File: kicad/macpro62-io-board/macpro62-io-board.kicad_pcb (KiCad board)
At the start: 6 copper layers, 101 x 173.6 mm, 146 parts, among them J1 IOB-HS1 MCIO 124 RA <- CB J3 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, J2 DISPLAY-LINK MCIO 74 RA <- Fa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, J25 ETH1 i226-V #1: ZJLQ-RJ45-SMD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, J26 ETH2 i226-V #2: ZJLQ-RJ45-SMD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, J28 Stock audio module connector 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, J29 Speaker 2P (stock lead; pitch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, J3 Stock PSU DC-out 12P (UNCONFI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, J30 Optional stock/remote power b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, J31 I/O-wall (821-2222) flex ZIF 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, J4 Stock PSU signal 6P (UNCONFIR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, J5 PSU pass-through -> BP J2 (12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, J6 IOB-LINK GH15 <- BP J6, J7 CONN_C fan + AirPort 2x20 @0.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, SW1 DNP with the stock 821-2222-A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, SW2 DIAG button, T1 ETH1 2.5G magnetics JASN V24P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, T2 ETH2 2.5G magnetics JASN V24P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, U1 TPS65994AD PD #1 (C1, C2), U11 TUSB1046A C1 alt-mode mux/red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, U12 TUSB1046A C2 alt-mode mux/red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, U13 TUSB1046A C3 alt-mode mux/red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, U14 TUSB1046A C4 alt-mode mux/red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, U15 TUSB1046A C5 alt-mode mux/red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, U16 TUSB1046A C6 alt-mode mux/red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, U2 TPS65994AD PD #2 (C3, C4), U21 TUSB1002A A1 10G redriver, U22 TUSB1002A A2 10G redriver, U23 TUSB1002A A3 10G redriver, U24 TUSB1002A A4 10G redriver, U25 USB-A A1 VBUS switch 1.5 A (S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, U26 USB-A A2 VBUS switch 1.5 A (S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, U27 USB-A A3 VBUS switch 1.5 A (S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, U28 USB-A A4 VBUS switch 1.5 A (S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, U3 TPS65994AD PD #3 (C5, C6), U30 Hall A (DRV5032 class) - posi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, U31 Hall B (DRV5032 class) - posi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, U32 CH334R hub H1b (C4-C6 + codec), U33 CH334R hub H2 (A1-A4) <- IOB-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, U34 CH334R hub H1a (C1-C3 + H1b) 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, U35 CH334R hub H3 on H2 port 4: A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, U4 PD #1 config SPI flash (W25Q8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, U40 TPS259824ON eFuse 12 V in (15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, U41 TPS56C215 5V_C buck (USB-C VB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, U42 TPS56C215 5V_A buck (USB-A VB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, U43 TLV62585 3V3 (3 A) from 5V_SYS, U50 i226-V 2.5GbE (PCIe x1 from H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, U51 i226-V NVM SPI flash (size pe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, U52 i226-V #2 2.5GbE (PCIe x1 fro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, U53 i226-V #2 NVM SPI flash, U6 PD #2 config SPI flash, U60 TDP158 HDMI 2.0 retimer (GPU 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, U61 1V1 LDO (TDP158 core), U7 PD #3 config SPI flash, U70 C-Media CM108B USB audio code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, U71 PAM8302A mono class-D 2.5 W (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, U80 TLC59116 16-ch I2C LED driver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, U81 LIS2DH12 accelerometer (rotat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, U82 BL24C64A IOB ID EEPROM @0x51, U83 TCA9517 I2C buffer (I2C_SYS <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, U84 74LVC1G07 PD_INT -> IOB_INT_N, U90 EMC2101 fan controller @0x4C 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, U91 ASM1182e PCIe Gen2 switch: up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, Y1 12 MHz hub crystal, Y2 12 MHz hub crystal, Y3 12 MHz hub crystal, Y4 25 MHz (i226-V), Y5 12 MHz (CM108B), Y6 25 MHz (i226-V #2), Y7 12 MHz hub crystal (H3)

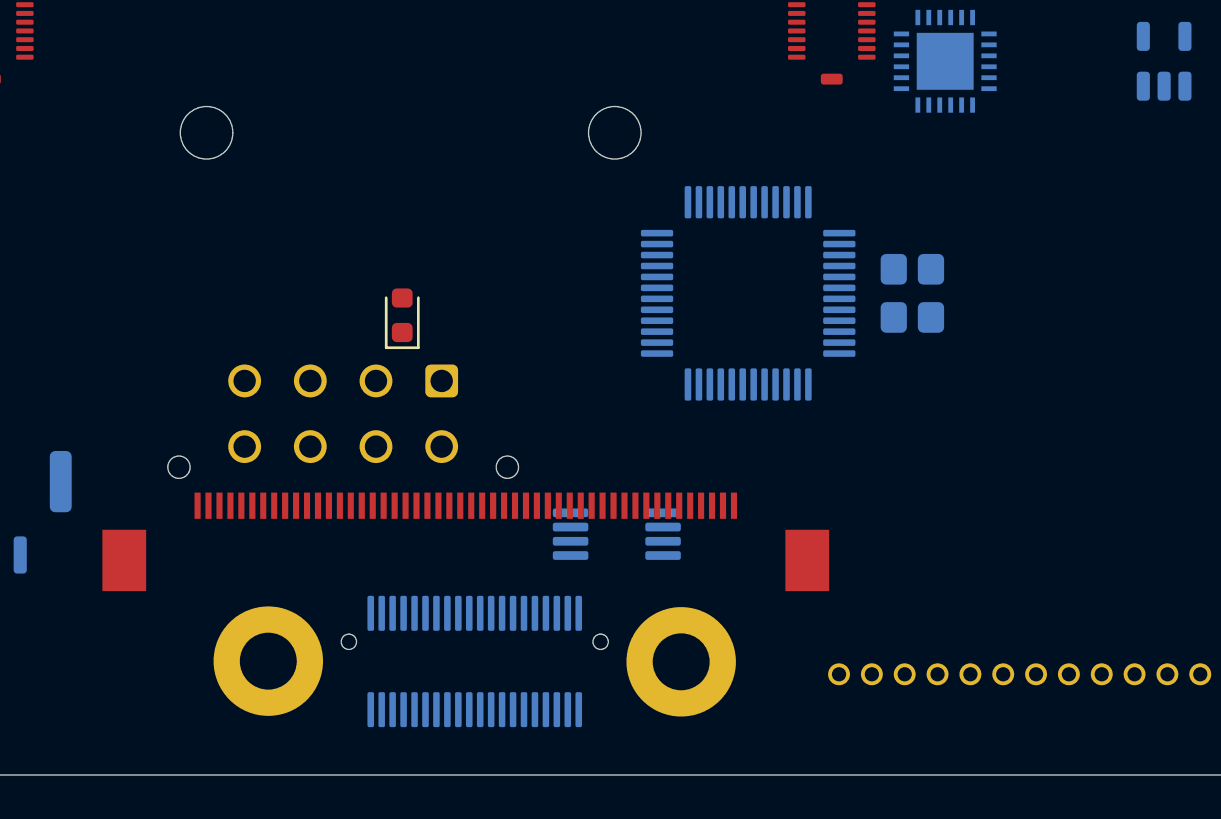
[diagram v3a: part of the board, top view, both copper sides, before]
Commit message: I/O: cover scan check (R inner ~102-110), fan antenna U.FL J8, T8 bracket keep-out, BCM94360 12+6 pinout on CONN_C
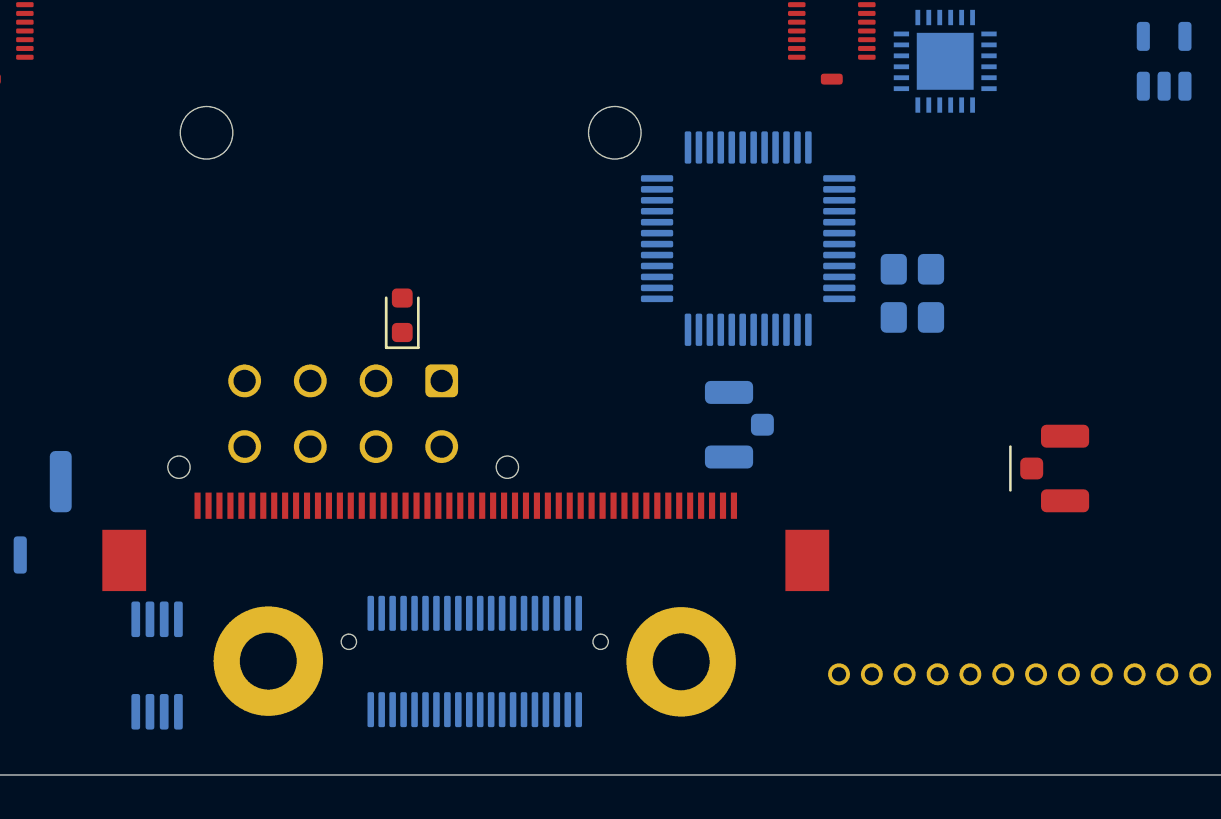
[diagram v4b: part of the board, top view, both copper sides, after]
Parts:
- added J8: Fan-assembly antenna coax: U.FL-R-SMT-1(10) C88373 (stock t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, MP62_IO:MP62_UFL_Hirose_U.FL-R-SMT-1, B.Cu at (102.6, 184.0)
- added J9: Optional antenna pass-through U.FL C88373 (50 ohm CPW from 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, MP62_IO:MP62_UFL_Hirose_U.FL-R-SMT-1, F.Cu at (117.0, 186.0)
- moved U90 21.8 mm to (76.0, 195.0), turned to 90 degrees
- moved U70 2.50 mm to (103.0, 175.5)
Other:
- board text added: "B: T8 fan-cable bracket keep-out (only J7, H14, H15)"

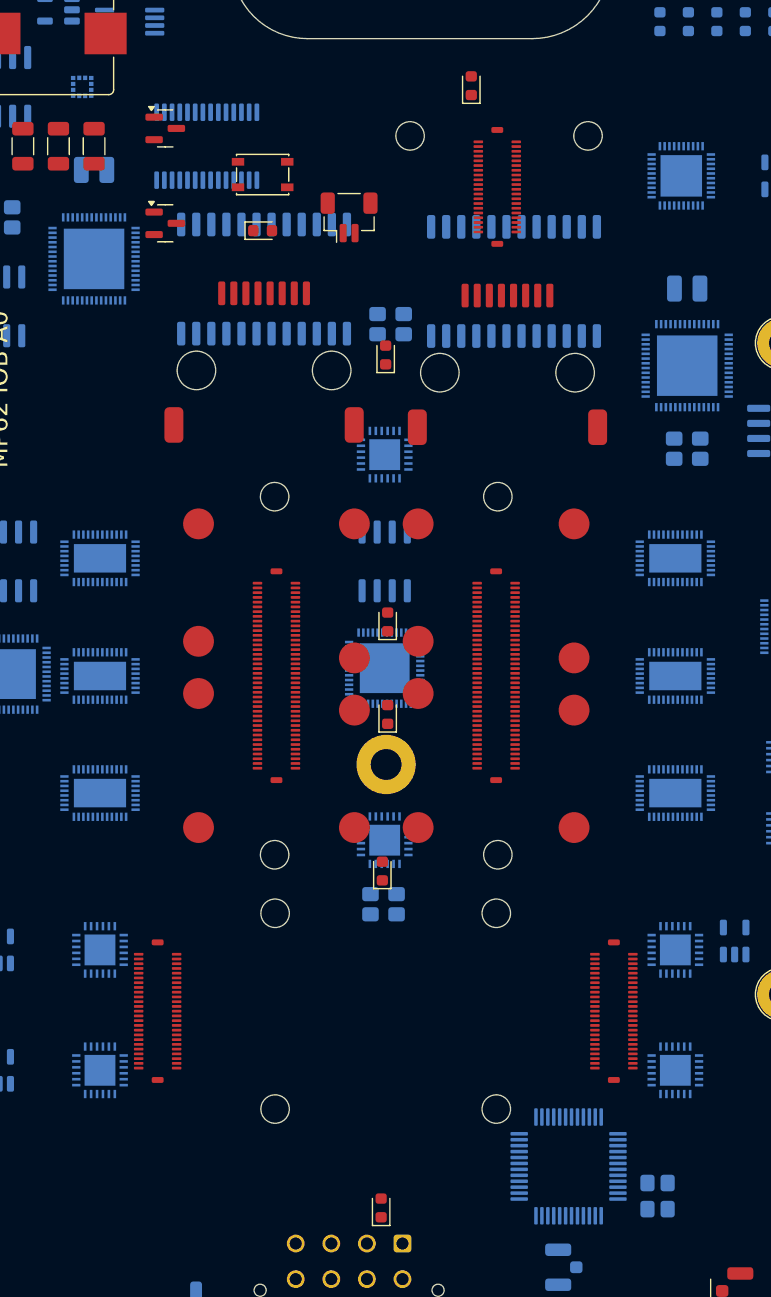
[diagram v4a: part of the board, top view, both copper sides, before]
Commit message: I/O: ports tilted 12.5 deg per stock, riser edge trims, USB-A B2B moved on top, outer-face plug seats, D21-D26 removed
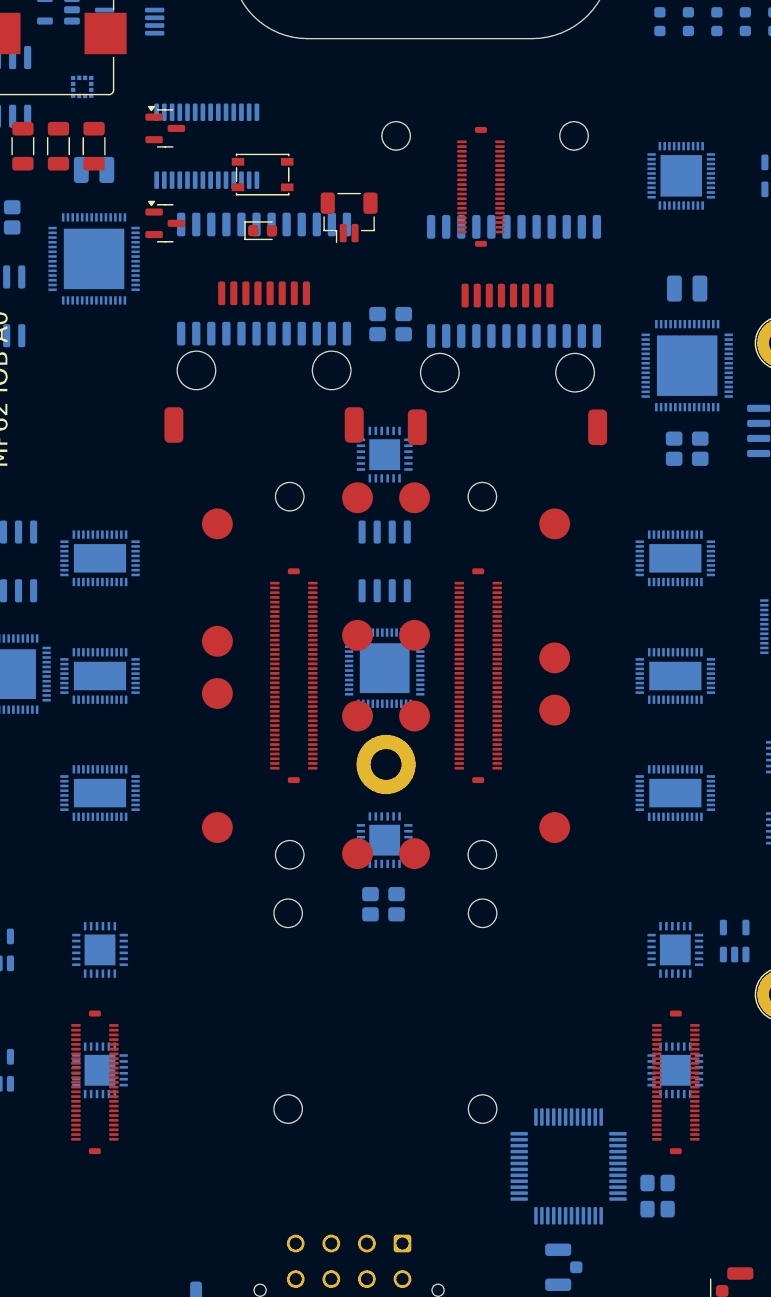
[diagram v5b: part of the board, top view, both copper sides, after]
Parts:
- removed D21: Light-pipe LED: HDMI label - DNP with the stock flex (its o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, MP62_IO:LED_0603_1608Metric
- removed D22: Light-pipe LED: ETH icon - DNP with the stock flex (its own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, MP62_IO:LED_0603_1608Metric
- removed D23: Light-pipe LED: USB-C icon upper - DNP with the stock flex 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, MP62_IO:LED_0603_1608Metric
- removed D24: Light-pipe LED: USB-C icon lower - DNP with the stock flex 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, MP62_IO:LED_0603_1608Metric
- removed D25: Light-pipe LED: USB icon - DNP with the stock flex (its own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, MP62_IO:LED_0603_1608Metric
- removed D26: Light-pipe LED: audio icons - DNP with the stock flex (its 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, MP62_IO:LED_0603_1608Metric
- JR1: value RC_H riser link (C, ports C1/C2/C3, tilt -5.27 deg): DF40C-80DS-0.4V(51) C312960 + flex jumper w/ 2 x DF40C-80DP plugs -> RC_H riser link (C, ports C1/C2/C3, tilt -12.50 deg): DF40C-80DS-0.4V(51) C312960 + flex jumper w/ 2 x DF40C-80DP plugs
- JR2: value RC_O riser link (C, ports C4/C5/C6, tilt 5.47 deg): DF40C-80DS-0.4V(51) C312960 + flex jumper w/ 2 x DF40C-80DP plugs -> RC_O riser link (C, ports C4/C5/C6, tilt 12.50 deg): DF40C-80DS-0.4V(51) C312960 + flex jumper w/ 2 x DF40C-80DP plugs
- JR3: value RA_H riser link (A, ports A1/A2, tilt -5.25 deg): DF40C-50DS-0.4V(51) TBC + flex jumper w/ 2 x DF40C-50DP plugs -> RA_H riser link (A, ports A1/A2, tilt -12.50 deg): DF40C-50DS-0.4V(51) TBC + flex jumper w/ 2 x DF40C-50DP plugs (U-tur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
- JR4: value RA_O riser link (A, ports A3/A4, tilt 5.51 deg): DF40C-50DS-0.4V(51) TBC + flex jumper w/ 2 x DF40C-50DP plugs -> RA_O riser link (A, ports A3/A4, tilt 12.50 deg): DF40C-50DS-0.4V(51) TBC + flex jumper w/ 2 x DF40C-50DP plugs (U-turn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
- JR5: value RH riser link (HDMI, ports HDMI, tilt -5.33 deg): DF40C-40DS-0.4V(51) TBC + flex jumper w/ 2 x DF40C-40DP plugs -> RH riser link (HDMI, ports HDMI, tilt -12.50 deg): DF40C-40DS-0.4V(51) TBC + flex jumper w/ 2 x DF40C-40DP plugs
- PG1: value RC_H pogo VBUS_C3, working height 5.94 -> RC_H pogo VBUS_C3, working height 4.79, length class P-S
- PG10: value RC_O pogo VBUS_C3, working height 7.14 -> RC_O pogo VBUS_C3, working height 7.38, length class P-L
- PG11: value RC_O pogo VBUS_C2, working height 5.88 -> RC_O pogo VBUS_C2, working height 4.77, length class P-S
- PG12: value RC_O pogo VBUS_C2, working height 7.14 -> RC_O pogo VBUS_C2, working height 7.38, length class P-L
- PG13: value RC_O pogo VBUS_C1, working height 5.88 -> RC_O pogo VBUS_C1, working height 4.77, length class P-S
- PG14: value RC_O pogo VBUS_C1, working height 7.14 -> RC_O pogo VBUS_C1, working height 7.38, length class P-L
- PG15: value RC_O pogo GND, working height 5.88 -> RC_O pogo GND, working height 4.77, length class P-S
- PG16: value RC_O pogo GND, working height 7.14 -> RC_O pogo GND, working height 7.38, length class P-L
- PG2: value RC_H pogo VBUS_C3, working height 7.15 -> RC_H pogo VBUS_C3, working height 7.41, length class P-L
- PG3: value RC_H pogo VBUS_C2, working height 5.94 -> RC_H pogo VBUS_C2, working height 4.79, length class P-S
- PG4: value RC_H pogo VBUS_C2, working height 7.15 -> RC_H pogo VBUS_C2, working height 7.41, length class P-L
- PG5: value RC_H pogo VBUS_C1, working height 5.94 -> RC_H pogo VBUS_C1, working height 4.79, length class P-S
- PG6: value RC_H pogo VBUS_C1, working height 7.15 -> RC_H pogo VBUS_C1, working height 7.41, length class P-L
- PG7: value RC_H pogo GND, working height 5.94 -> RC_H pogo GND, working height 4.79, length class P-S
- PG8: value RC_H pogo GND, working height 7.15 -> RC_H pogo GND, working height 7.41, length class P-L
- PG9: value RC_O pogo VBUS_C3, working height 5.88 -> RC_O pogo VBUS_C3, working height 4.77, length class P-S
- moved JR4 8.00 mm to (63.1, 168.4)
- moved JR3 7.96 mm to (112.0, 168.4)
- moved PG2 2.22 mm to (90.0, 149.1)
- moved PG6 2.22 mm to (90.0, 119.1)
- moved PG10 2.22 mm to (85.2, 119.1)
- moved PG14 2.22 mm to (85.2, 149.1)
- moved PG4 1.92 mm to (90.0, 137.5)
- moved PG12 1.92 mm to (85.2, 130.7)
- moved PG1 1.64 mm to (101.8, 146.9)
- moved PG3 1.64 mm to (101.8, 132.6)
- moved PG5 1.64 mm to (101.8, 121.3)
- moved PG7 1.64 mm to (101.8, 137.0)
- moved PG11 1.59 mm to (73.4, 135.6)
- moved PG13 1.59 mm to (73.4, 146.9)
- moved PG15 1.59 mm to (73.4, 131.2)
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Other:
- board text added: "RA_H riser -12.5 deg"
- board text added: "RA_O riser 12.5 deg"
- board text added: "RC_H riser -12.5 deg"
- board text added: "RC_O riser 12.5 deg"
- board text added: "RH riser -12.5 deg"
- board text removed: "RA_H riser -5.2 deg"
- board text removed: "RA_O riser 5.5 deg"
- board text removed: "RC_H riser -5.3 deg"
- board text removed: "RC_O riser 5.5 deg"
- board text removed: "RH riser -5.3 deg"
